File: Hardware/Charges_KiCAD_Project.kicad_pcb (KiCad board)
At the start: 4 copper layers, 80 x 87.2 mm, 44 parts, among them IC1 TP124005-2, IC2 STM32L562VET6Q, J1 TB002-500-04BE, J2 TB002-500-04BE, J3 L717SDC37P1ACH4F, Q1 SI7232DN-T1-GE3, Q2 SI7232DN-T1-GE3, U1 MS5607-02BA, Y1 32mhz

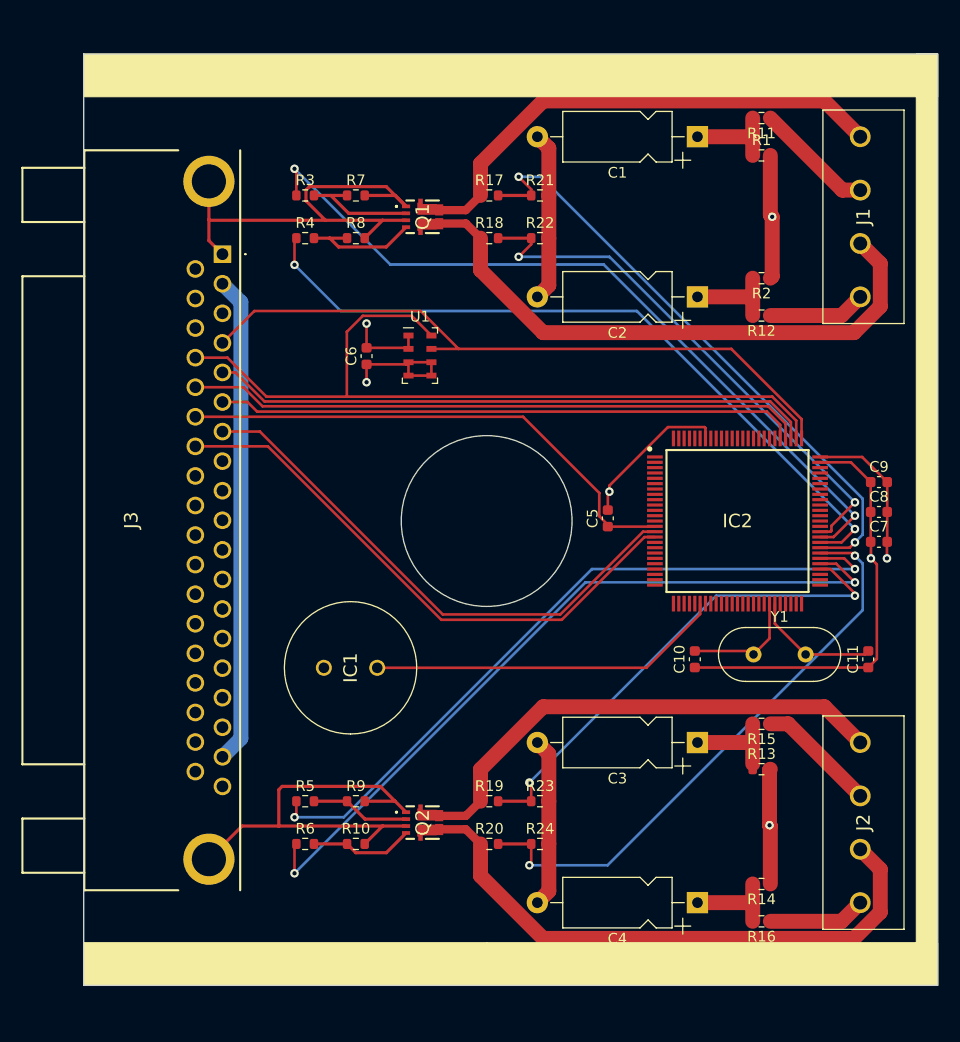
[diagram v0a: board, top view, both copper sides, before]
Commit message: Changes to PCB size and components
PCB size was changed by adding 3mm to the top and bottom, the screw terminal was switched to a 90 degree angle one, and the libraries were updated
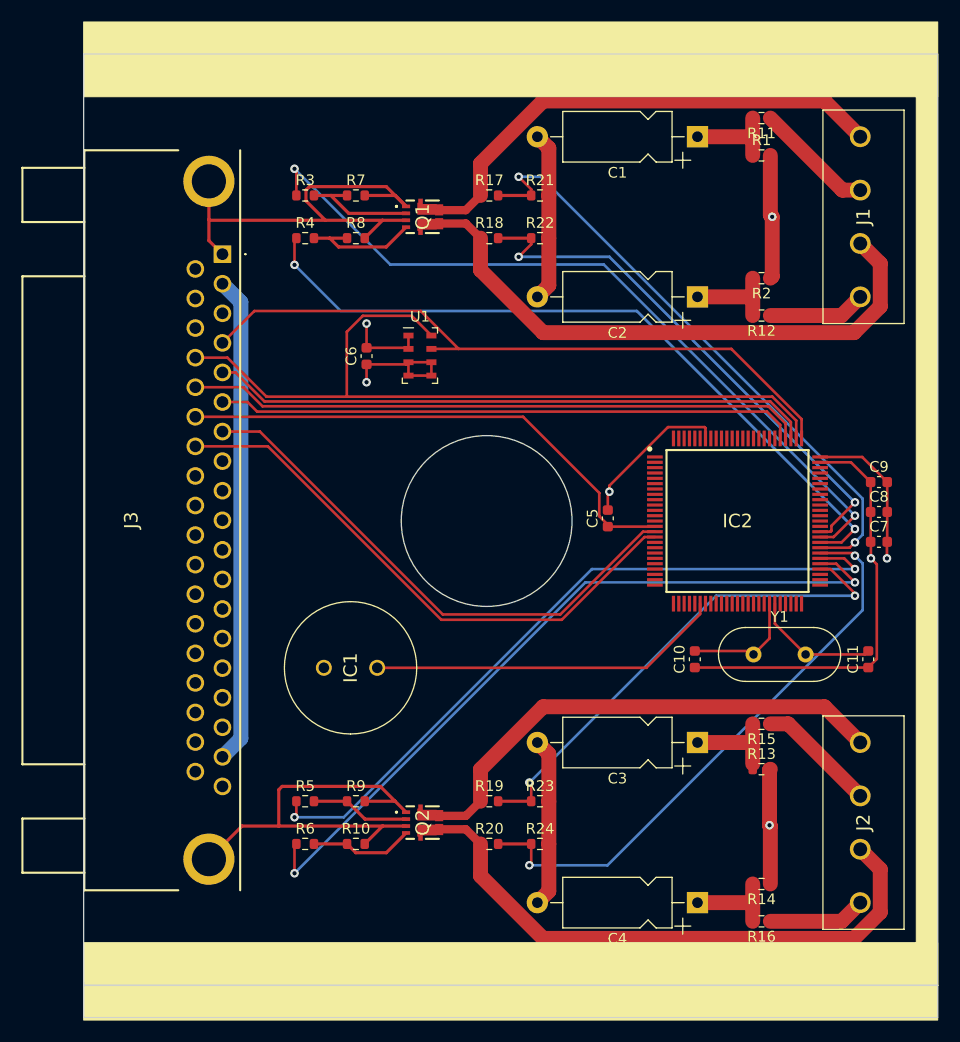
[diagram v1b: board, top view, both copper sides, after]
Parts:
- J1, J2: footprint SamacSys_Parts:TB00250004BE -> RDT_Custom_Footprints:TB00250004BE
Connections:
- IC2 pad 1: Net-(IC2-Pad1) -> (no net)
- IC2 pad 10: Net-(IC2-Pad10) -> (no net)
- IC2 pad 100: Net-(IC2-Pad100) -> (no net)
- IC2 pad 11: Net-(IC2-Pad11) -> (no net)
- IC2 pad 12: Net-(IC2-Pad12) -> (no net)
- IC2 pad 13: Net-(IC2-Pad13) -> (no net)
- IC2 pad 17: Net-(IC2-Pad17) -> (no net)
- IC2 pad 18: Net-(IC2-Pad18) -> (no net)
- IC2 pad 19: Net-(IC2-Pad19) -> (no net)
- IC2 pad 2: Net-(IC2-Pad2) -> (no net)
- IC2 pad 20: Net-(IC2-Pad20) -> (no net)
- IC2 pad 21: Net-(IC2-Pad21) -> (no net)
- IC2 pad 22: Net-(IC2-Pad22) -> (no net)
- IC2 pad 23: Net-(IC2-Pad23) -> (no net)
- IC2 pad 24: Net-(IC2-Pad24) -> (no net)
- IC2 pad 25: Net-(IC2-Pad25) -> (no net)
- IC2 pad 26: Net-(IC2-Pad26) -> (no net)
- IC2 pad 27: Net-(IC2-Pad27) -> (no net)
- IC2 pad 28: Net-(IC2-Pad28) -> (no net)
- IC2 pad 29: Net-(IC2-Pad29) -> (no net)
- IC2 pad 3: Net-(IC2-Pad3) -> (no net)
- IC2 pad 30: Net-(IC2-Pad30) -> (no net)
- IC2 pad 32: Net-(IC2-Pad32) -> (no net)
- IC2 pad 33: Net-(IC2-Pad33) -> (no net)
- IC2 pad 34: Net-(IC2-Pad34) -> (no net)
- IC2 pad 35: Net-(IC2-Pad35) -> (no net)
- IC2 pad 36: Net-(IC2-Pad36) -> (no net)
- IC2 pad 37: Net-(IC2-Pad37) -> (no net)
- IC2 pad 38: Net-(IC2-Pad38) -> (no net)
- IC2 pad 39: Net-(IC2-Pad39) -> (no net)
- IC2 pad 4: Net-(IC2-Pad4) -> (no net)
- IC2 pad 40: Net-(IC2-Pad40) -> (no net)
- IC2 pad 41: Net-(IC2-Pad41) -> (no net)
- IC2 pad 42: Net-(IC2-Pad42) -> (no net)
- IC2 pad 43: Net-(IC2-Pad43) -> (no net)
- IC2 pad 46: Net-(IC2-Pad46) -> (no net)
- IC2 pad 47: Net-(IC2-Pad47) -> (no net)
- IC2 pad 48: Net-(IC2-Pad48) -> (no net)
- IC2 pad 49: Net-(IC2-Pad49) -> (no net)
- IC2 pad 5: Net-(IC2-Pad5) -> (no net)
- IC2 pad 50: Net-(IC2-Pad50) -> (no net)
- IC2 pad 51: Net-(IC2-Pad51) -> (no net)
- IC2 pad 52: Net-(IC2-Pad52) -> (no net)
- IC2 pad 53: Net-(IC2-Pad53) -> (no net)
- IC2 pad 6: Net-(IC2-Pad6) -> (no net)
- IC2 pad 62: Net-(IC2-Pad62) -> (no net)
- IC2 pad 63: Net-(IC2-Pad63) -> (no net)
- IC2 pad 64: Net-(IC2-Pad64) -> (no net)
- IC2 pad 65: Net-(IC2-Pad65) -> (no net)
- IC2 pad 66: Net-(IC2-Pad66) -> (no net)
- IC2 pad 67: Net-(IC2-Pad67) -> (no net)
- IC2 pad 68: Net-(IC2-Pad68) -> (no net)
- IC2 pad 69: Net-(IC2-Pad69) -> (no net)
- IC2 pad 7: Net-(IC2-Pad7) -> (no net)
- IC2 pad 70: Net-(IC2-Pad70) -> (no net)
- IC2 pad 71: Net-(IC2-Pad71) -> (no net)
- IC2 pad 72: Net-(IC2-Pad72) -> (no net)
- IC2 pad 73: Net-(IC2-Pad73) -> (no net)
- IC2 pad 8: Net-(IC2-Pad8) -> (no net)
- IC2 pad 81: Net-(IC2-Pad81) -> (no net)
- IC2 pad 82: Net-(IC2-Pad82) -> (no net)
- IC2 pad 83: Net-(IC2-Pad83) -> (no net)
- IC2 pad 84: Net-(IC2-Pad84) -> (no net)
- IC2 pad 85: Net-(IC2-Pad85) -> (no net)
- IC2 pad 86: Net-(IC2-Pad86) -> (no net)
- IC2 pad 87: Net-(IC2-Pad87) -> (no net)
- IC2 pad 88: Net-(IC2-Pad88) -> (no net)
- IC2 pad 89: Net-(IC2-Pad89) -> (no net)
- IC2 pad 9: Net-(IC2-Pad9) -> (no net)
- IC2 pad 90: Net-(IC2-Pad90) -> (no net)
- IC2 pad 91: Net-(IC2-Pad91) -> (no net)
- IC2 pad 92: Net-(IC2-Pad92) -> (no net)
- IC2 pad 93: Net-(IC2-Pad93) -> (no net)
- IC2 pad 95: Net-(IC2-Pad95) -> (no net)
- IC2 pad 96: Net-(IC2-Pad96) -> (no net)
- IC2 pad 97: Net-(IC2-Pad97) -> (no net)
- IC2 pad 98: Net-(IC2-Pad98) -> (no net)
- IC2 pad 99: Net-(IC2-Pad99) -> (no net)
- J3 pad 10: Net-(J3-Pad10) -> (no net)
- J3 pad 11: Net-(J3-Pad11) -> (no net)
- J3 pad 12: Net-(J3-Pad12) -> (no net)
- J3 pad 13: Net-(J3-Pad13) -> (no net)
- J3 pad 14: Net-(J3-Pad14) -> (no net)
- J3 pad 15: Net-(J3-Pad15) -> (no net)
- J3 pad 16: Net-(J3-Pad16) -> (no net)
- J3 pad 17: Net-(J3-Pad17) -> (no net)
- J3 pad 21: /Sheet61A437B4/t_mosi -> (no net)
- J3 pad 22: /Sheet61A437B4/t_clk -> (no net)
- J3 pad 27: Net-(J3-Pad27) -> (no net)
- J3 pad 28: Net-(J3-Pad28) -> (no net)
- J3 pad 29: Net-(J3-Pad29) -> (no net)
- J3 pad 3: /Sheet61A437B4/t_miso -> (no net)
- J3 pad 30: Net-(J3-Pad30) -> (no net)
- J3 pad 31: Net-(J3-Pad31) -> (no net)
- J3 pad 32: Net-(J3-Pad32) -> (no net)
- J3 pad 33: Net-(J3-Pad33) -> (no net)
- J3 pad 34: Net-(J3-Pad34) -> (no net)
- J3 pad 35: Net-(J3-Pad35) -> (no net)
- J3 pad 36: Net-(J3-Pad36) -> (no net)
- J3 pad 8: Net-(J3-Pad8) -> (no net)
- J3 pad 9: Net-(J3-Pad9) -> (no net)
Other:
- board size 80 x 87.2 mm -> 80 x 90.2 mm

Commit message: Replaced passive component footprints with handsolder variants
Most components unaffected, redesign was needed around SI7232DN chips
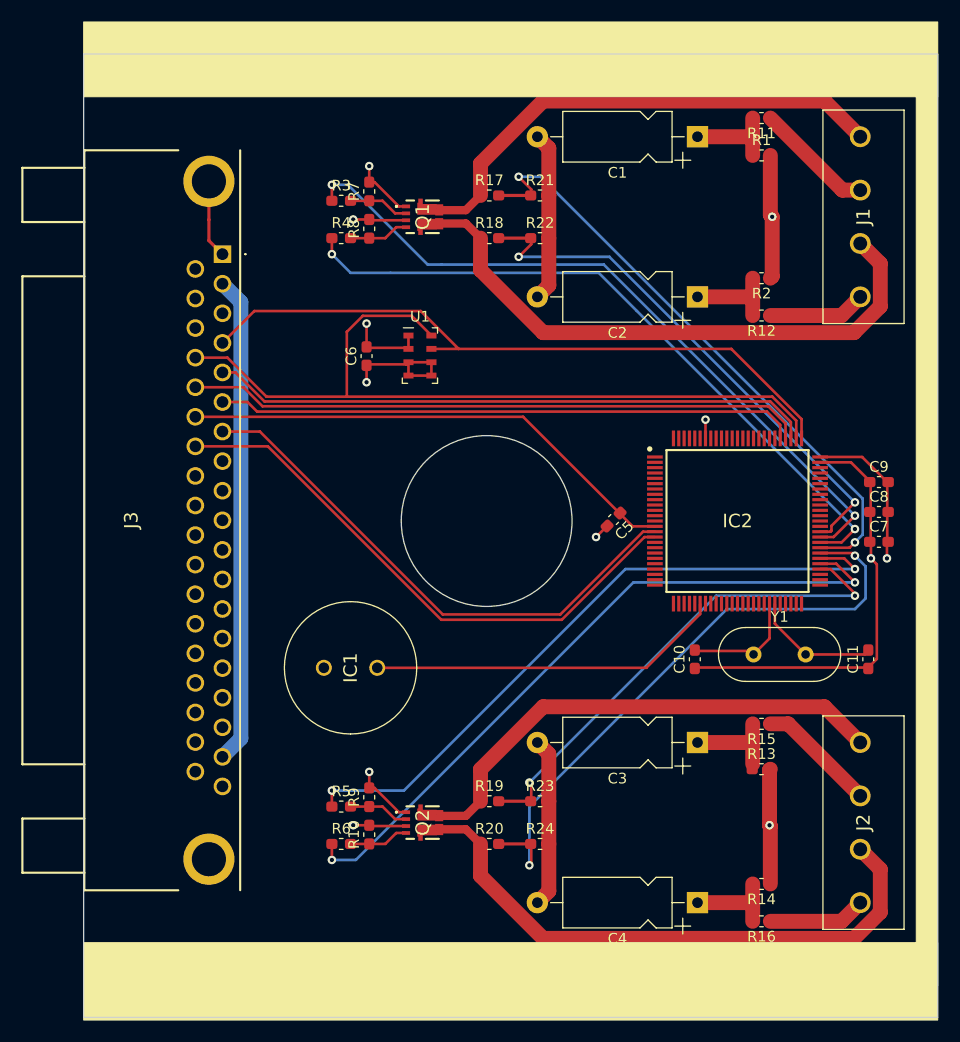
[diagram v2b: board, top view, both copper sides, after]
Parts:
- C10, C11, C5, C6, C7, C8, C9: footprint Capacitor_SMD:C_0603_1608Metric -> Capacitor_SMD:C_0603_1608Metric_Pad1.08x0.95mm_HandSolder
- J1, J2: value TB002-500-04BE -> 796684-4
- R1, R10, R11, R12, R13, R14, R15, R16, R17, R18, R19, R2, R20, R21, R22, R23, R24, R3, R4, R5, R6, R7, R8, R9: footprint Resistor_SMD:R_0603_1608Metric -> Resistor_SMD:R_0603_1608Metric_Pad1.05x0.95mm_HandSolder
- moved R3 3.41 mm to (112.6, 66.2)
- moved R5 3.41 mm to (112.6, 123.0)
- moved R4 3.38 mm to (112.6, 69.8)
- moved R6 3.38 mm to (112.6, 126.5)
- moved R10 1.53 mm to (115.2, 125.6), turned to 90 degrees
- moved R8 1.53 mm to (115.2, 68.9), turned to 90 degrees
- moved R7 1.31 mm to (115.2, 65.4), turned to 90 degrees
- moved R9 1.31 mm to (115.2, 122.1), turned to 90 degrees
- moved C5 0.55 mm to (138.1, 96.1), turned to 225 degrees
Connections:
- IC2 pad 1: (no net) -> Net-(IC2-Pad1)
- IC2 pad 10: (no net) -> Net-(IC2-Pad10)
- IC2 pad 100: (no net) -> Net-(IC2-Pad100)
- IC2 pad 11: (no net) -> Net-(IC2-Pad11)
- IC2 pad 12: (no net) -> Net-(IC2-Pad12)
- IC2 pad 13: (no net) -> Net-(IC2-Pad13)
- IC2 pad 17: (no net) -> Net-(IC2-Pad17)
- IC2 pad 18: (no net) -> Net-(IC2-Pad18)
- IC2 pad 19: (no net) -> Net-(IC2-Pad19)
- IC2 pad 2: (no net) -> Net-(IC2-Pad2)
- IC2 pad 20: (no net) -> Net-(IC2-Pad20)
- IC2 pad 21: (no net) -> Net-(IC2-Pad21)
- IC2 pad 22: (no net) -> Net-(IC2-Pad22)
- IC2 pad 23: (no net) -> Net-(IC2-Pad23)
- IC2 pad 24: (no net) -> Net-(IC2-Pad24)
- IC2 pad 25: (no net) -> Net-(IC2-Pad25)
- IC2 pad 26: (no net) -> Net-(IC2-Pad26)
- IC2 pad 27: (no net) -> Net-(IC2-Pad27)
- IC2 pad 28: (no net) -> Net-(IC2-Pad28)
- IC2 pad 29: (no net) -> Net-(IC2-Pad29)
- IC2 pad 3: (no net) -> Net-(IC2-Pad3)
- IC2 pad 30: (no net) -> Net-(IC2-Pad30)
- IC2 pad 32: (no net) -> Net-(IC2-Pad32)
- IC2 pad 33: (no net) -> Net-(IC2-Pad33)
- IC2 pad 34: (no net) -> Net-(IC2-Pad34)
- IC2 pad 35: (no net) -> Net-(IC2-Pad35)
- IC2 pad 36: (no net) -> Net-(IC2-Pad36)
- IC2 pad 37: (no net) -> Net-(IC2-Pad37)
- IC2 pad 38: (no net) -> Net-(IC2-Pad38)
- IC2 pad 39: (no net) -> Net-(IC2-Pad39)
- IC2 pad 4: (no net) -> Net-(IC2-Pad4)
- IC2 pad 40: (no net) -> Net-(IC2-Pad40)
- IC2 pad 41: (no net) -> Net-(IC2-Pad41)
- IC2 pad 42: (no net) -> Net-(IC2-Pad42)
- IC2 pad 43: (no net) -> Net-(IC2-Pad43)
- IC2 pad 46: (no net) -> Net-(IC2-Pad46)
- IC2 pad 47: (no net) -> Net-(IC2-Pad47)
- IC2 pad 48: (no net) -> Net-(IC2-Pad48)
- IC2 pad 49: (no net) -> Net-(IC2-Pad49)
- IC2 pad 5: (no net) -> Net-(IC2-Pad5)
- IC2 pad 50: (no net) -> Net-(IC2-Pad50)
- IC2 pad 51: (no net) -> Net-(IC2-Pad51)
- IC2 pad 52: (no net) -> Net-(IC2-Pad52)
- IC2 pad 53: (no net) -> Net-(IC2-Pad53)
- IC2 pad 6: (no net) -> Net-(IC2-Pad6)
- IC2 pad 62: (no net) -> Net-(IC2-Pad62)
- IC2 pad 63: (no net) -> Net-(IC2-Pad63)
- IC2 pad 64: (no net) -> Net-(IC2-Pad64)
- IC2 pad 65: (no net) -> Net-(IC2-Pad65)
- IC2 pad 66: (no net) -> Net-(IC2-Pad66)
- IC2 pad 67: (no net) -> Net-(IC2-Pad67)
- IC2 pad 68: (no net) -> Net-(IC2-Pad68)
- IC2 pad 69: (no net) -> Net-(IC2-Pad69)
- IC2 pad 7: (no net) -> Net-(IC2-Pad7)
- IC2 pad 70: (no net) -> Net-(IC2-Pad70)
- IC2 pad 71: (no net) -> Net-(IC2-Pad71)
- IC2 pad 72: (no net) -> Net-(IC2-Pad72)
- IC2 pad 73: (no net) -> Net-(IC2-Pad73)
- IC2 pad 8: (no net) -> Net-(IC2-Pad8)
- IC2 pad 81: (no net) -> Net-(IC2-Pad81)
- IC2 pad 82: (no net) -> Net-(IC2-Pad82)
- IC2 pad 83: (no net) -> Net-(IC2-Pad83)
- IC2 pad 84: (no net) -> Net-(IC2-Pad84)
- IC2 pad 85: (no net) -> Net-(IC2-Pad85)
- IC2 pad 86: (no net) -> Net-(IC2-Pad86)
- IC2 pad 87: (no net) -> Net-(IC2-Pad87)
- IC2 pad 88: (no net) -> Net-(IC2-Pad88)
- IC2 pad 89: (no net) -> Net-(IC2-Pad89)
- IC2 pad 9: (no net) -> Net-(IC2-Pad9)
- IC2 pad 90: (no net) -> Net-(IC2-Pad90)
- IC2 pad 91: (no net) -> Net-(IC2-Pad91)
- IC2 pad 92: (no net) -> Net-(IC2-Pad92)
- IC2 pad 93: (no net) -> Net-(IC2-Pad93)
- IC2 pad 95: (no net) -> Net-(IC2-Pad95)
- IC2 pad 96: (no net) -> Net-(IC2-Pad96)
- IC2 pad 97: (no net) -> Net-(IC2-Pad97)
- IC2 pad 98: (no net) -> Net-(IC2-Pad98)
- IC2 pad 99: (no net) -> Net-(IC2-Pad99)
- J3 pad 10: (no net) -> Net-(J3-Pad10)
- J3 pad 11: (no net) -> Net-(J3-Pad11)
- J3 pad 12: (no net) -> Net-(J3-Pad12)
- J3 pad 13: (no net) -> Net-(J3-Pad13)
- J3 pad 14: (no net) -> Net-(J3-Pad14)
- J3 pad 15: (no net) -> Net-(J3-Pad15)
- J3 pad 16: (no net) -> Net-(J3-Pad16)
- J3 pad 17: (no net) -> Net-(J3-Pad17)
- J3 pad 21: (no net) -> /DSUB_37_Male/t_mosi
- J3 pad 22: (no net) -> /DSUB_37_Male/t_clk
- J3 pad 27: (no net) -> Net-(J3-Pad27)
- J3 pad 28: (no net) -> Net-(J3-Pad28)
- J3 pad 29: (no net) -> Net-(J3-Pad29)
- J3 pad 3: (no net) -> /DSUB_37_Male/t_miso
- J3 pad 30: (no net) -> Net-(J3-Pad30)
- J3 pad 31: (no net) -> Net-(J3-Pad31)
- J3 pad 32: (no net) -> Net-(J3-Pad32)
- J3 pad 33: (no net) -> Net-(J3-Pad33)
- J3 pad 34: (no net) -> Net-(J3-Pad34)
- J3 pad 35: (no net) -> Net-(J3-Pad35)
- J3 pad 36: (no net) -> Net-(J3-Pad36)
- J3 pad 8: (no net) -> Net-(J3-Pad8)
- J3 pad 9: (no net) -> Net-(J3-Pad9)
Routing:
- net GND: track 186.4 -> 116.3 mm, vias 3 -> 8
- net Net-(Q1-Pad4): track 11.4 -> 5.62 mm
- net /Fire_D: track 70.6 -> 65.3 mm
- net /Fire_A: track 72.6 -> 67.4 mm
- net Net-(Q1-Pad2): track 10.8 -> 5.69 mm
- net /Fire_C: track 67.4 -> 62.8 mm
- net /Fire_B: track 69.1 -> 64.9 mm
- net Net-(Q2-Pad4): track 9.73 -> 5.62 mm
- net Net-(Q2-Pad2): track 9.32 -> 5.69 mm
- net /Sense_D: track 55.1 -> 58.0 mm
- net /NRST: track 48.7 -> 47.3 mm
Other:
- outline, holes or cut-outs redrawn
